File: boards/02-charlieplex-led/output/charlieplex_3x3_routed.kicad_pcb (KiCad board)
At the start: 2 copper layers, 50 x 55 mm, 14 parts, among them U1 MCU

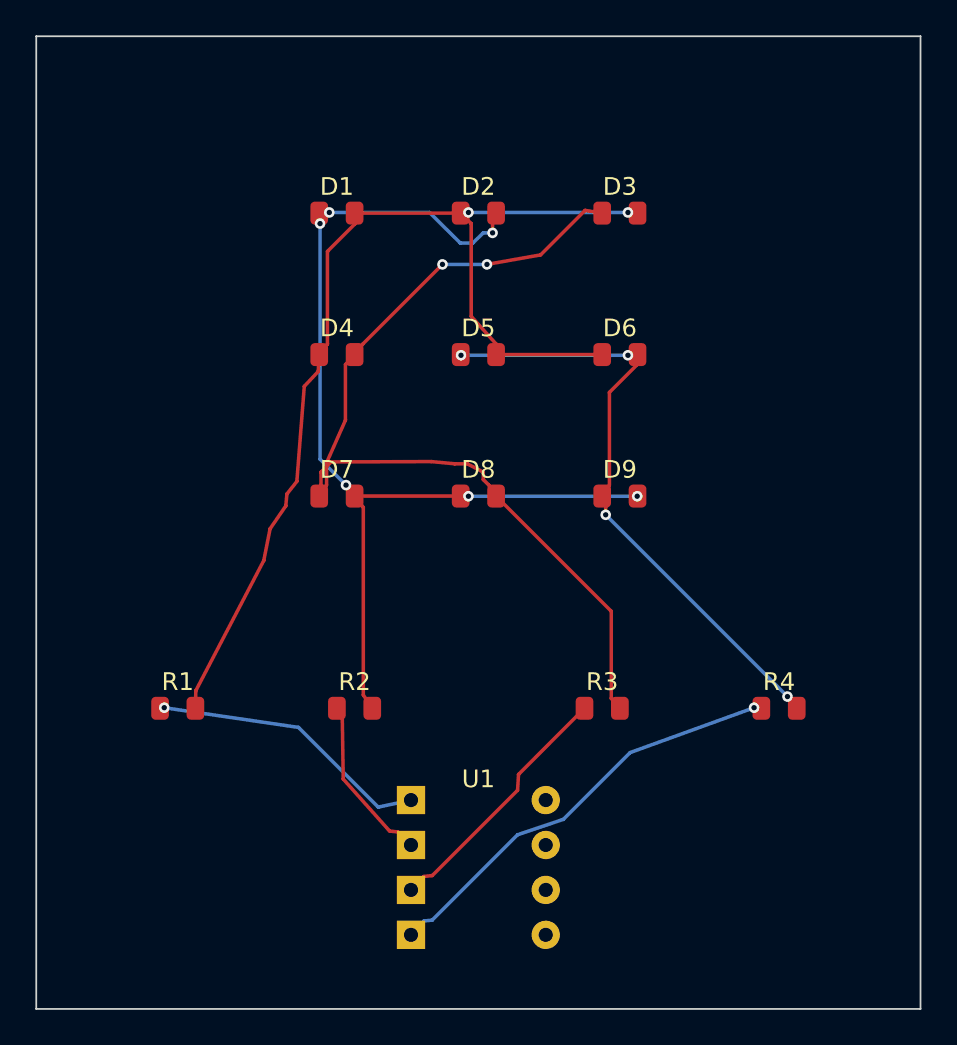
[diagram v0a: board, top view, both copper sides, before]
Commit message: fix(router): extend narrow-channel halo to exterior side of same-component plane-net pads (closes #2902)
The 44 `clearance_pad_segment` errors on board-04's U2 west edge originate
in the main router extending escape stubs across F.Cu, clipping plane-net
pads on the same component. No escape-phase predicate could prevent this
(see closed PR #2897 for the diagnostic).

Extends `_apply_narrow_channel_halo` in grid.py to cover the exterior
corridor adjacent to same-component plane-net pads (`pad.net != 0`), in
addition to the existing inter-pad channel coverage from #2879. Width
follows the existing clearance + segment-trace-width margin.

Per-board regression suite re-run; routed PCBs regenerated for boards 01-04.

Closes #2902

Co-Authored-By: Claude Opus 4.7 (1M context) <noreply@anthropic.com>
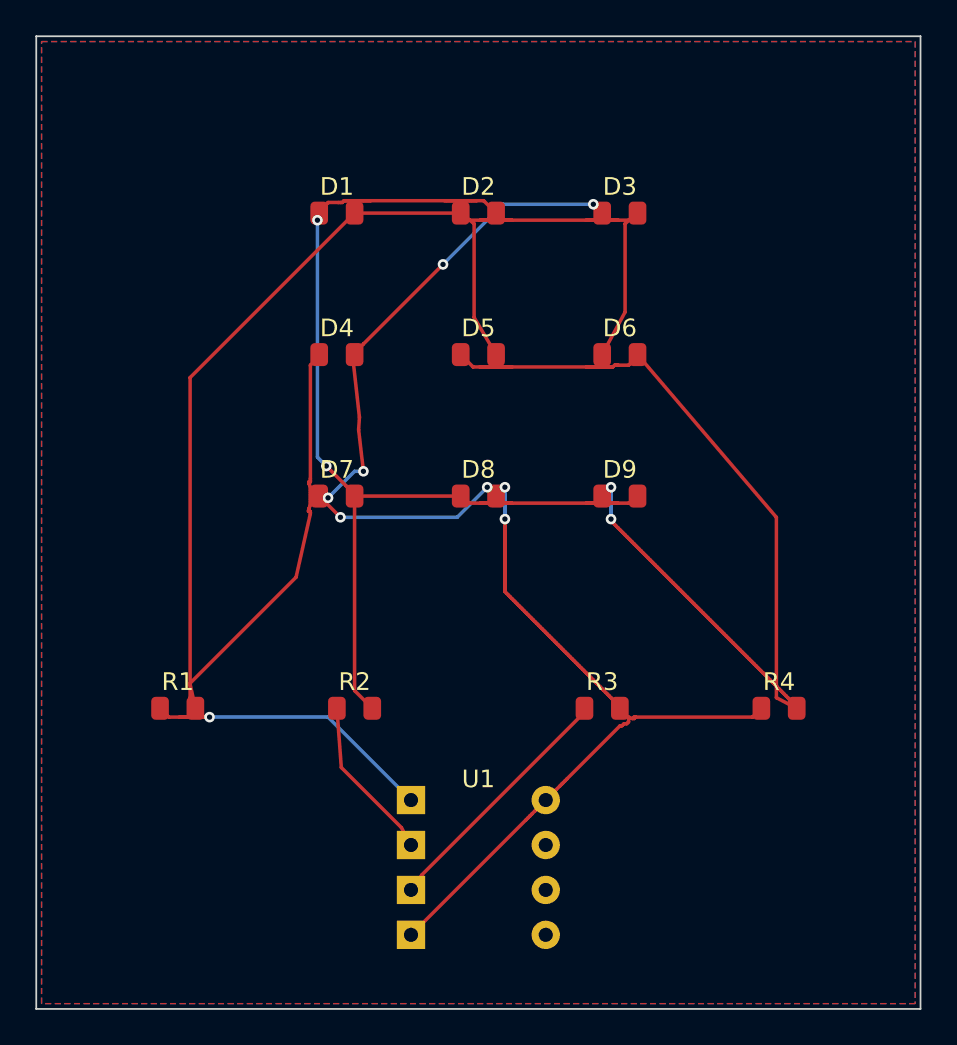
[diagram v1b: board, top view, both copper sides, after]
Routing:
- net NODE_A: track 61.4 -> 88.6 mm, vias 2 -> 0
- net NODE_D: track 35.3 -> 51.7 mm, vias 4 -> 2
- net NODE_C: track 53.2 -> 54.8 mm, vias 2 -> 8
- net LINE_D: track 24.3 -> 25.4 mm, vias 1 -> 0
- net NODE_B: track 57.0 -> 56.2 mm, vias 6 -> 2
- added copper zone on B.Cu, net GND
- added copper zone on F.Cu, net VCC
